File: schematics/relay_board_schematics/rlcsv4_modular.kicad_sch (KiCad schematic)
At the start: 43 parts, among them J1 Programming Header, P1 ACT_PWR, P2 ACT_PWR, P3 ACTUATOR, Q1 MMBF170, Q2 MMBF170, SW1 SW_DIP_x04, U1 SPST_POWER_RELAY, U2 PIC16F1826-ISO, U3 dpdt_relay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

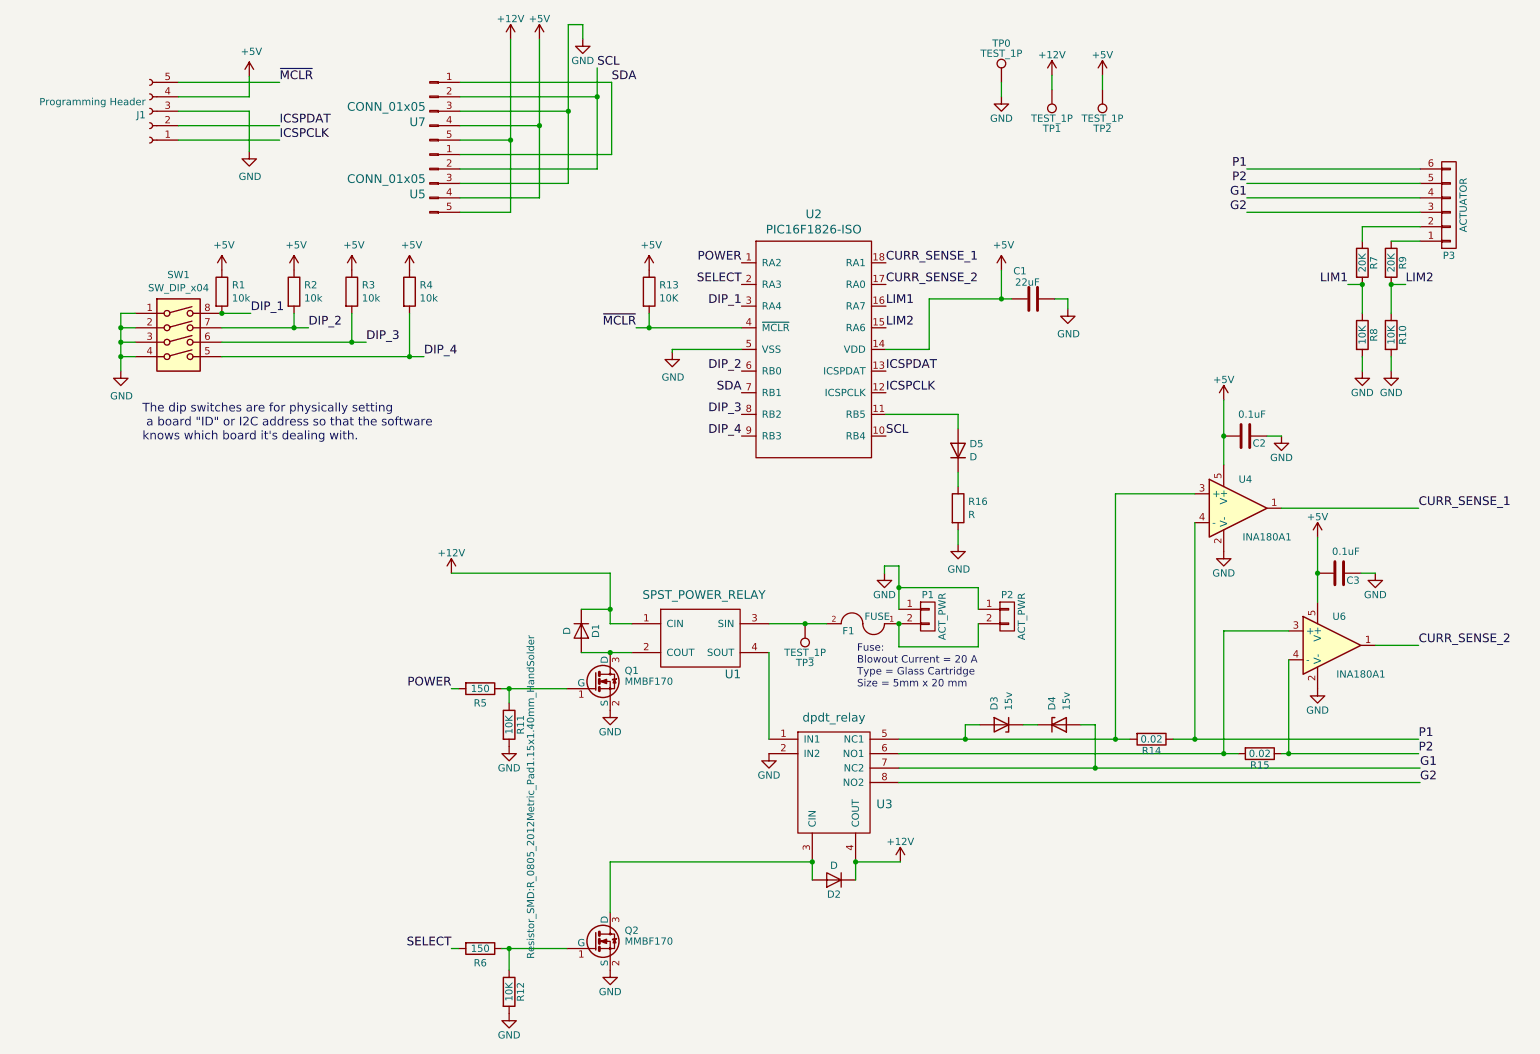
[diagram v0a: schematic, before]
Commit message: clean up on wire spacing, power errors, add diode to actuator
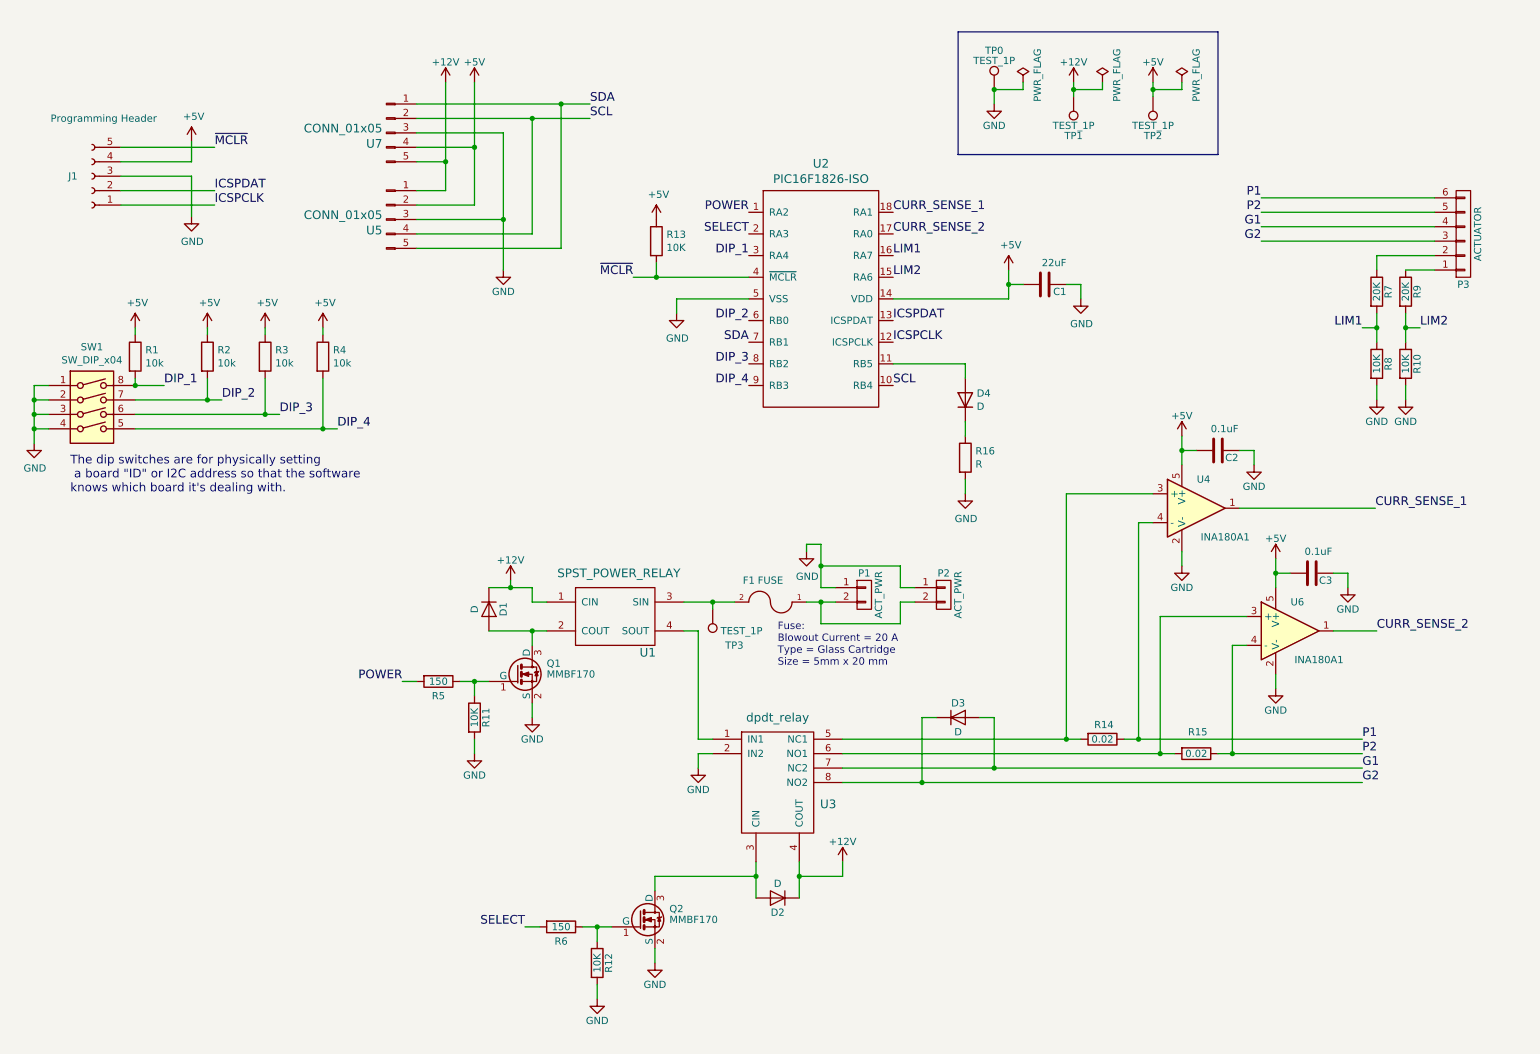
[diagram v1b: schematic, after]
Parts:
- removed D3, D4: 15v, symbol Device:D_Zener
- added D3: D, Diode_THT:D_DO-35_SOD27_P7.62mm_Horizontal, symbol rlcsv4_modular-rescue:D-rlcsv3_modular-rescue
- renumbered D5 to D4
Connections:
- net +12V: now also U5.1; no longer U5.5
- net +5V: now also U5.2; no longer U5.4
- net G1: now also D3.2 (A)
- net G2: now also D3.1 (K)
- net SCL: now also U5.4; no longer U5.2
- net SDA: now also U5.5; no longer U5.1
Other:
- title: RLCSv4 -> RLCS Relay_Board
- moved on the sheet: C1, C2, C3, D1, D2, D4, F1, J1, P1, P2, P3, Q1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
